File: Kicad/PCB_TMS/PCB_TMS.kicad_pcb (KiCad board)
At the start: 2 copper layers, 30 parts, among them J1 Conn_ARM_JTAG_SWD_10, SW1 SW_DPDT_x2, U1 STM32F030F4Px, U2 MCP9700T-ETT, U3 M24C01-FDW, Y1 20MHz

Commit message: Routage v1
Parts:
- moved TP1 71.2 mm to (169.2, 76.2)
- moved TP2 67.5 mm to (166.3, 73.1)
- moved TP7 63.1 mm to (166.6, 96.9)
- moved D2 59.1 mm to (163.7, 73.0), turned to -90 degrees
- moved R1 58.7 mm to (166.1, 78.1)
- moved R7 56.0 mm to (162.5, 71.7), turned to 180 degrees
- moved TP6 53.0 mm to (166.5, 93.8)
- moved C4 52.0 mm to (175.3, 85.8)
- moved TP3 51.4 mm to (176.2, 79.6), turned to 180 degrees
- moved R6 47.8 mm to (161.5, 73.5), turned to 90 degrees
- moved U2 46.8 mm to (175.2, 83.1), turned to 180 degrees
- moved R3 46.5 mm to (158.3, 82.9), turned to 90 degrees
- moved 1uF1 45.4 mm to (160.9, 89.8), turned to 90 degrees
- moved R2 44.8 mm to (164.5, 78.1), turned to 180 degrees
- moved D1 44.7 mm to (161.5, 75.2), turned to -90 degrees
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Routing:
- net TEMP: track 0.00 -> 55.3 mm
- net +3.3V: track 0.00 -> 40.9 mm
- net RST: track 0.00 -> 39.7 mm
- net E0: track 0.00 -> 27.3 mm
- net E1: track 0.00 -> 25.8 mm
- net Net-(C6-Pad2): track 0.00 -> 22.1 mm
- net SWDIO/TMS: track 0.00 -> 14.8 mm
- net Net-(C5-Pad2): track 0.00 -> 14.5 mm
- net SWCLM/TCK: track 0.00 -> 12.9 mm
- net E2: track 0.00 -> 12.3 mm
- net WC: track 0.00 -> 9.12 mm
- net LED0: track 0.00 -> 8.25 mm
- net SCL: track 0.00 -> 8.02 mm
- net LED1: track 0.00 -> 7.71 mm
- net BOOT: track 0.00 -> 7.55 mm
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
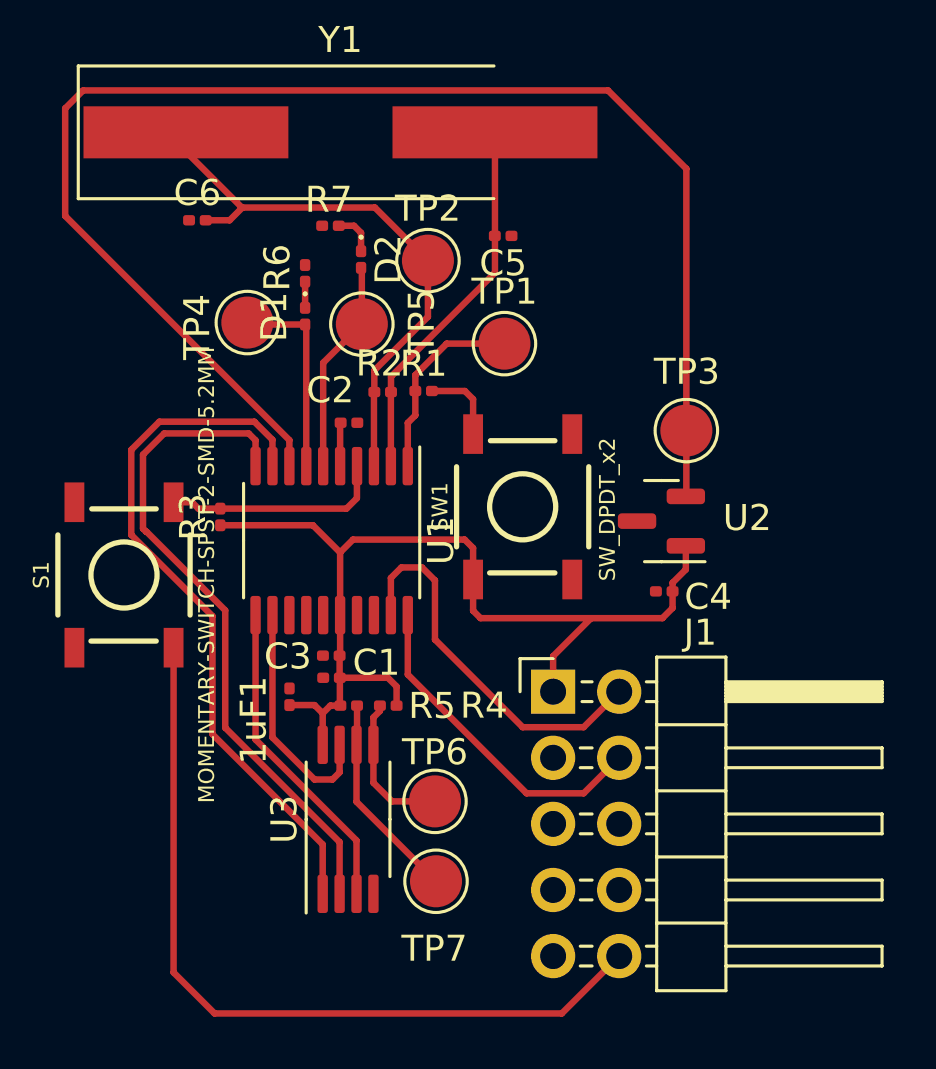
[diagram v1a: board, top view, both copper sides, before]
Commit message: Changement d'empreintes
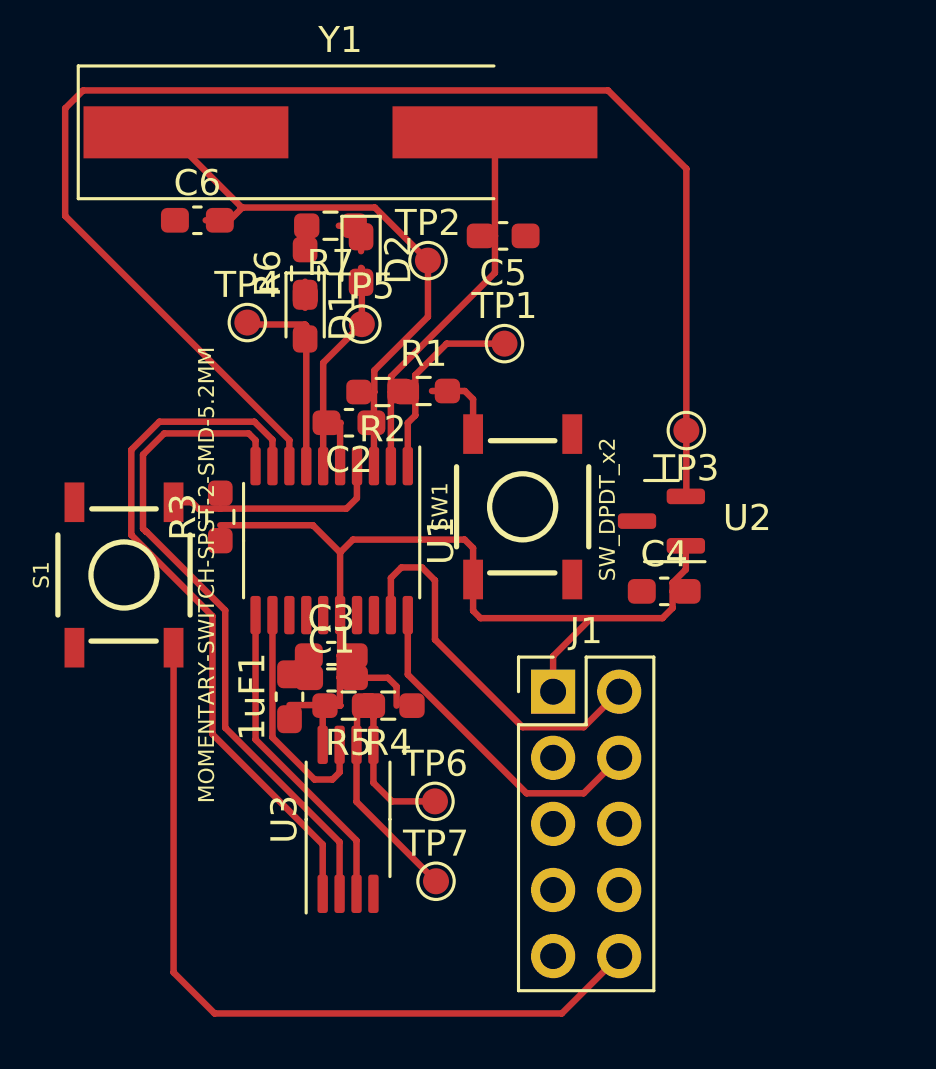
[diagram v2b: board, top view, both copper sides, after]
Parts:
- 1uF1, C1, C2, C3, C4, C5, C6: footprint Capacitor_SMD:C_0201_0603Metric -> Capacitor_SMD:C_0603_1608Metric_Pad1.08x0.95mm_HandSolder
- D1, D2: footprint Diode_SMD:D_0201_0603Metric -> Diode_SMD:D_0603_1608Metric_Pad1.05x0.95mm_HandSolder
- J1: footprint Connector_PinHeader_2.54mm:PinHeader_2x05_P2.54mm_Horizontal -> Connector_PinHeader_2.54mm:PinHeader_2x05_P2.54mm_Vertical
- R1, R2, R3, R4, R5, R6, R7: footprint Resistor_SMD:R_0201_0603Metric -> Resistor_SMD:R_0603_1608Metric_Pad0.98x0.95mm_HandSolder
- TP1, TP2, TP3, TP4, TP5, TP6, TP7: footprint TestPoint:TestPoint_Pad_D2.0mm -> TestPoint:TestPoint_Pad_D1.0mm
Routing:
- net BOOT: track 7.55 -> 0.00 mm
- net Net-(C5-Pad2): track 14.5 -> 22.0 mm
- net SCL: track 8.02 -> 13.8 mm
- net SDA: track 5.73 -> 0.00 mm
- net LED0: track 8.25 -> 9.92 mm
- net +3.3V: track 40.9 -> 39.3 mm

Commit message: PCB Routage fini
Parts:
- removed R3: 1k, Resistor_SMD:R_0603_1608Metric_Pad0.98x0.95mm_HandSolder
- removed S1: MOMENTARY-SWITCH-SPST-2-SMD-5.2MM, Switches:TACTILE_SWITCH_SMD_5.2MM
- added C7: 0.1µF, Capacitor_SMD:C_0603_1608Metric_Pad1.08x0.95mm_HandSolder, F.Cu at (149.7, 93.5)
- added C8: 100nF, Capacitor_SMD:C_0603_1608Metric_Pad1.08x0.95mm_HandSolder, F.Cu at (135.9, 101.9)
- added C9: 100nF, Capacitor_SMD:C_0603_1608Metric_Pad1.08x0.95mm_HandSolder, F.Cu at (129.4, 90.9)
- added SW2: SW_Push, Button_Switch_SMD:SW_SPST_SKQG_WithStem, F.Cu at (147.2, 87.2)
- C3: value 4.7uF -> 0.1uF
- SW1: footprint Switches:TACTILE_SWITCH_SMD_5.2MM -> Connector_PinHeader_2.54mm:PinHeader_1x03_P2.54mm_Vertical
- moved TP3 45.1 mm to (131.8, 87.9), turned to 0 degrees
- moved U2 43.6 mm to (132.3, 90.8)
- moved C4 43.5 mm to (132.5, 93.4)
- moved SW1 36.8 mm to (141.1, 105.4)
- moved C5 35.6 mm to (148.8, 101.3), turned to 0 degrees
- moved TP1 35.1 mm to (145.9, 102.5), turned to -90 degrees
- moved R1 33.4 mm to (143.2, 102.4), turned to 180 degrees
- moved Y1 33.2 mm to (153.2, 99.9), turned to -90 degrees
- moved TP7 32.8 mm to (133.8, 96.8)
- moved R4 31.8 mm to (135.9, 103.5), turned to 0 degrees
- moved TP5 31.1 mm to (135.0, 87.5), turned to 90 degrees
- moved D2 31.0 mm to (135.0, 84.8)
- moved TP4 30.0 mm to (131.2, 85.8), turned to -90 degrees
- moved D1 29.9 mm to (133.2, 84.8)
- moved R5 29.7 mm to (135.0, 99.5), turned to -90 degrees
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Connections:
- U1 pad 10: E1 -> SWCLM/TCK
- U1 pad 11: E2 -> LED0
- U1 pad 12: WC -> LED1
- U1 pad 13: unconnected-(U1-Pad13) -> TEMP
- U1 pad 19: SWDIO/TMS -> WC
- U1 pad 20: SWCLM/TCK -> unconnected-(U1-Pad20)
- U1 pad 6: LED0 -> E2
- U1 pad 7: LED1 -> E1
- U1 pad 8: TEMP -> E0
- U1 pad 9: E0 -> SWDIO/TMS
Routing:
- net TEMP: track 55.3 -> 7.88 mm
- net GND: track 0.00 -> 31.2 mm, vias 0 -> 3
- net +3.3V: track 39.3 -> 59.3 mm
- net SDA: track 0.00 -> 15.8 mm
- net E1: track 25.8 -> 10.9 mm
- net E0: track 27.3 -> 13.1 mm
- net BOOT: track 0.00 -> 9.57 mm
- net SWDIO/TMS: track 14.8 -> 6.03 mm
- net RST: track 39.7 -> 33.3 mm
- net Net-(C5-Pad2): track 22.0 -> 16.2 mm
- net SWCLM/TCK: track 12.9 -> 7.50 mm
- net SCL: track 13.8 -> 9.16 mm
- net LED0: track 9.92 -> 6.15 mm
- net E2: track 12.3 -> 8.98 mm
- net WC: track 9.12 -> 6.29 mm
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- added copper zone on F.Cu, net GND
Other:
- board outline added: 30.3 x 34.7 mm
- board text added: "Louis Amaury"

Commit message: Génération gerber
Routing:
- added copper zone on F.Cu, net (none)
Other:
- board size 30.3 x 34.7 mm -> 30.3 x 35.7 mm
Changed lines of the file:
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@@
       (outputformat 1)
       (mirror false)
-      (drillshape 1)
+      (drillshape 0)
       (scaleselection 1)
-      (outputdirectory "")
+      (outputdirectory "Gerber/")
     )
   )
@@
     )
   )
-  (gr_rect (start 127.25 75.95) (end 157.6 110.65) (layer "Edge.Cuts") (width 0.1) (fill none))
+  (gr_rect (start 127.25 75.95) (end 157.6 111.666) (layer "Edge.Cuts") (width 0.1) (fill none))
   (gr_text "Louis\nAmaury" (at 131.45 107.3) (layer "F.Cu")
     (effects (font (size 1 1) (thickness 0.25)))
@@
     (polygon
       (pts
-        (xy 157.6 110.65)
-        (xy 127.25 110.65)
+        (xy 157.6 111.666)
+        (xy 127.25 111.666)
         (xy 127.25 75.95)
         (xy 157.6 75.95)
       )
     )
+  )
+  (zone (net 0) (net_name "") (layer "F.Cu") (hatch edge 0.508)
+    (priority 1)
+    (connect_pads (clearance 0))
+    (min_thickness 0.254) (filled_areas_thickness no)
+    (fill yes (thermal_gap 0.508) (thermal_bridge_width 0.508))
+    (polygon
+      (pts
+        (xy 155.829 110.109)
+        (xy 150.495 110.109)
+        (xy 150.495 89.535)
+        (xy 155.829 89.535)
+      )
+    )

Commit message: correction PCB
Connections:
- U1 pad 10: SWCLM/TCK -> unconnected-(U1-Pad10)
- U1 pad 19: WC -> SWDIO/TMS
- U1 pad 20: unconnected-(U1-Pad20) -> SWCLM/TCK
- U1 pad 9: SWDIO/TMS -> unconnected-(U1-Pad9)
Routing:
- net SWCLM/TCK: track 7.50 -> 15.9 mm, vias 0 -> 2
- net WC: track 6.29 -> 0.00 mm
- net unconnected-(U1-Pad9): track 0.00 -> 6.03 mm
- net SWDIO/TMS: track 6.03 -> 9.00 mm, vias 0 -> 1
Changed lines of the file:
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@@
   (net 23 "WC")
   (net 24 "unconnected-(U1-Pad14)")
-  (net 25 "unconnected-(U1-Pad20)")
+  (net 25 "unconnected-(U1-Pad9)")
+  (net 26 "unconnected-(U1-Pad10)")
   (footprint "TestPoint:TestPoint_Pad_D1.0mm" (layer "F.Cu")
     (at 133.8 96.8)
@@
       (net 20 "E0") (pinfunction "PA2") (pintype "bidirectional"))
     (pad "9" smd roundrect (at -2.8625 2.275 180) (size 1.475 0.4) (layers "F.Cu" "F.Paste" "F.Mask") (roundrect_rratio 0.25)
-      (net 9 "SWDIO{slash}TMS") (pinfunction "PA3") (pintype "bidirectional"))
+      (net 25 "unconnected-(U1-Pad9)") (pinfunction "PA3") (pintype "bidirectional"))
     (pad "10" smd roundrect (at -2.8625 2.925 180) (size 1.475 0.4) (layers "F.Cu" "F.Paste" "F.Mask") (roundrect_rratio 0.25)
-      (net 10 "SWCLM{slash}TCK") (pinfunction "PA4") (pintype "bidirectional"))
+      (net 26 "unconnected-(U1-Pad10)") (pinfunction "PA4") (pintype "bidirectional"))
     (pad "11" smd roundrect (at 2.8625 2.925 180) (size 1.475 0.4) (layers "F.Cu" "F.Paste" "F.Mask") (roundrect_rratio 0.25)
       (net 8 "LED0") (pinfunction "PA5") (pintype "bidirectional"))
@@
       (net 17 "SDA") (pinfunction "PA10") (pintype "bidirectional"))
     (pad "19" smd roundrect (at 2.8625 -2.275 180) (size 1.475 0.4) (layers "F.Cu" "F.Paste" "F.Mask") (roundrect_rratio 0.25)
-      (net 23 "WC") (pinfunction "PA13") (pintype "bidirectional"))
+      (net 9 "SWDIO{slash}TMS") (pinfunction "PA13") (pintype "bidirectional"))
     (pad "20" smd roundrect (at 2.8625 -2.925 180) (size 1.475 0.4) (layers "F.Cu" "F.Paste" "F.Mask") (roundrect_rratio 0.25)
-      (net 25 "unconnected-(U1-Pad20)") (pinfunction "PA14") (pintype "bidirectional"))
+      (net 10 "SWCLM{slash}TCK") (pinfunction "PA14") (pintype "bidirectional"))
     (model "${KICAD6_3DMODEL_DIR}/Package_SO.3dshapes/TSSOP-20_4.4x6.5mm_P0.65mm.wrl"
       (offset (xyz 0 0 0))
@@
   (via (at 134.975 93.575) (size 0.8) (drill 0.4) (layers "F.Cu" "B.Cu") (free) (net 2))
   (via (at 141.2 98.3) (size 0.8) (drill 0.4) (layers "F.Cu" "B.Cu") (free) (net 2))
-  (segment (start 134.975 93.575) (end 139.7 98.3) (width 0.25) (layer "B.Cu") (net 2))
+  (segment (start 134.975 93.575) (end 134.975 97.275) (width 0.25) (layer "B.Cu") (net 2))
   (segment (start 138.975 100.525) (end 141.2 98.3) (width 0.25) (layer "B.Cu") (net 2))
+  (segment (start 134.975 97.275) (end 138.2 100.5) (width 0.25) (layer "B.Cu") (net 2))
   (segment (start 138.2 100.525) (end 138.975 100.525) (width 0.25) (layer "B.Cu") (net 2))
-  (segment (start 139.7 98.3) (end 141.2 98.3) (width 0.25) (layer "B.Cu") (net 2))
+  (segment (start 138.2 100.5) (end 138.2 100.525) (width 0.25) (layer "B.Cu") (net 2))
   (segment (start 149.6625 99.6875) (end 149.7 99.65) (width 0.25) (layer "F.Cu") (net 3))
   (segment (start 148.5 99.65) (end 149.7 99.65) (width 0.25) (layer "F.Cu") (net 3))
@@
   (segment (start 135 88.55) (end 135 87.55) (width 0.25) (layer "F.Cu") (net 8))
   (segment (start 135 85.703) (end 135.028 85.675) (width 0.25) (layer "F.Cu") (net 8))
-  (segment (start 140.455 91.705) (end 139.135 90.385) (width 0.25) (layer "F.Cu") (net 9))
-  (segment (start 142.5625 91.705) (end 140.455 91.705) (width 0.25) (layer "F.Cu") (net 9))
-  (segment (start 139.135 90.385) (end 139.135 88.325) (width 0.25) (layer "F.Cu") (net 9))
+  (via (at 136.55 96.25) (size 0.4) (drill 0.3) (layers "F.Cu" "B.Cu") (net 9))
+  (segment (start 138.15 94.65) (end 138.15 89.31) (width 0.25) (layer "B.Cu") (net 9))
+  (segment (start 136.55 96.25) (end 138.15 94.65) (width 0.25) (layer "B.Cu") (net 9))
+  (segment (start 138.15 89.31) (end 139.135 88.325) (width 0.25) (layer "B.Cu") (net 9))
   (segment (start 142.5625 91.055) (end 141.305 91.055) (width 0.25) (layer "F.Cu") (net 10))
   (segment (start 142.5625 91.055) (end 142.6175 91) (width 0.25) (layer "F.Cu") (net 10))
@@
   (segment (start 141.305 91.055) (end 140.31 90.06) (width 0.25) (layer "F.Cu") (net 10))
   (segment (start 140.31 86.96) (end 139.135 85.785) (width 0.25) (layer "F.Cu") (net 10))
+  (via (at 137.2 96.9) (size 0.4) (drill 0.3) (layers "F.Cu" "B.Cu") (net 10))
+  (via (at 141.305 91.055) (size 0.4) (drill 0.3) (layers "F.Cu" "B.Cu") (net 10))
+  (segment (start 137.2 96.9) (end 138.8 95.3) (width 0.25) (layer "B.Cu") (net 10))
+  (segment (start 138.8 95.3) (end 138.8 92.15) (width 0.25) (layer "B.Cu") (net 10))
+  (segment (start 138.8 92.15) (end 139.895 91.055) (width 0.25) (layer "B.Cu") (net 10))
+  (segment (start 139.895 91.055) (end 141.305 91.055) (width 0.25) (layer "B.Cu") (net 10))
   (segment (start 143.85 76.9) (end 149 82.05) (width 0.25) (layer "F.Cu") (net 14))
   (segment (start 142.5625 94.955) (end 143.755 94.955) (width 0.25) (layer "F.Cu") (net 14))
@@
   (segment (start 142.5625 99.025) (end 140.8 99.025) (width 0.25) (layer "F.Cu") (net 22))
   (segment (start 140.45 98.675) (end 140.45 94.35) (width 0.25) (layer "F.Cu") (net 22))
-  (segment (start 138.105 96.255) (end 136.8375 96.255) (width 0.25) (layer "F.Cu") (net 23))
-  (segment (start 138.5 99.3) (end 138.5 96.65) (width 0.25) (layer "F.Cu") (net 23))
-  (segment (start 136.8375 99.675) (end 138.125 99.675) (width 0.25) (layer "F.Cu") (net 23))
-  (segment (start 138.5 96.65) (end 138.105 96.255) (width 0.25) (layer "F.Cu") (net 23))
-  (segment (start 138.125 99.675) (end 138.5 99.3) (width 0.25) (layer "F.Cu") (net 23))
+  (segment (start 140.455 91.705) (end 139.135 90.385) (width 0.25) (layer "F.Cu") (net 25))
+  (segment (start 142.5625 91.705) (end 140.455 91.705) (width 0.25) (layer "F.Cu") (net 25))
+  (segment (start 139.135 90.385) (end 139.135 88.325) (width 0.25) (layer "F.Cu") (net 25))
   (zone (net 2) (net_name "GND") (layer "F.Cu") (hatch edge 0.508)
     (connect_pads (clearance 0.3))
